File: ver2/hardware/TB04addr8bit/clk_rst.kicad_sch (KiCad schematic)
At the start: 29 parts, among them SW4 SW_DIP_x04, SW5 SW_SPDT, SW6 SW_Push, SW7 SW_Push, U12 4060, U17 74HC14, Y1 32.768KHz

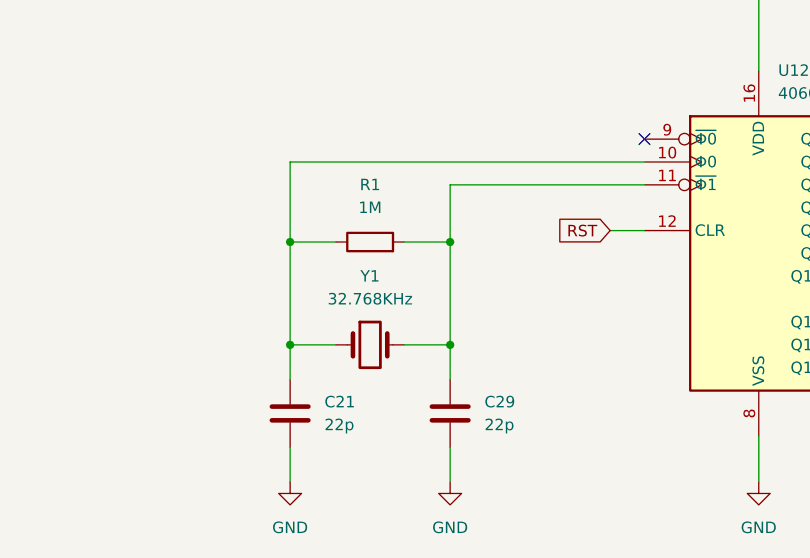
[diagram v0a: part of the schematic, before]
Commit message: ver2: レジスタファイル(RS00/RS01)とルート配線・発振回路定数を追加
- clk_rst: 74HC4060発振のRf=10M/Rs=220K/C=22p×2に確定
- RS00/RS01: R0-R7の具体回路(74HC161×4+74LS253×4)を追加
  ※図面は74LS253だがシンボル都合で実装はHC(74HC253)
- ルート: 書込デコード/読出セレクト/RegAddrSrc MUX/データ入出力の
  外側グルーを配線(DI/DOa/DOb/Reg_WE0-7/sel_a)
- PC_mAddrは作業中(Reg_WE8-11未結線)

Co-Authored-By: Claude Opus 4.8 <noreply@anthropic.com>
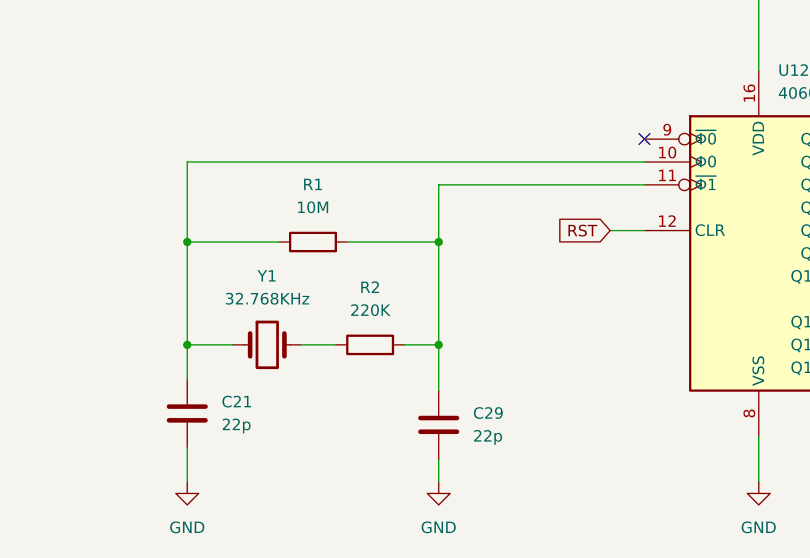
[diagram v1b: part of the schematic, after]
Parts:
- added R2: 220K, symbol Device:R
- R1: value 1M -> 10M
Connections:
- net at C29.1, R1.2, U12.11 (~{Φ1}): now also R2.2; no longer Y1.2
- new net: R2.1, Y1.2
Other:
- moved on the sheet: C21, C29, R1, Y1
